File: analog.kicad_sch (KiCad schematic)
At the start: 37 parts, among them J2 Conn_02x01, J3 Conn_02x01, J4 Conn_02x01, J5 Conn_02x01, J6 Screw_Terminal_01x02, U2 INA241A1xD, U3 INA241A1xD, U4 INA241A1xD, U5 INA241A1xD, U6 ADS131A04, Y2 16.384 MHz

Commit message: Initial release A1
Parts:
- C25, C27: value 10pF -> 30pF
- R4, R5, R6, R7: value 13.7R -> 13R; footprint Resistor_SMD:R_1210_3225Metric -> libpt:R_1206_3216Metric
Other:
- note added: "Resistors should be .1%"
- note added: "Voltage range: 13*10G*.025A = 3.25V max .1^2 * 13 = 130 mW (before fuse trips)"
- note removed: "Re-check crystal footprint when crystal is chosen"
- note removed: "Voltage range: 13.7R*10G*.024A = 3.288V max .1^2 * 13.7 = 137 mW (before fuse trips)"
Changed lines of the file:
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@@
 	(title_block
 		(title "PT DAQ")
-		(date "2026-01-01")
+		(date "2026-01-12")
 		(rev "1A")
 		(company "Aggie Propulsion and Rocketry Lab")
@@
 		)
 	)
-	(text "Voltage range:\n13.7R*10G*.024A = 3.288V max\n.1^2 * 13.7 = 137 mW (before fuse trips)"
+	(text "Voltage range:\n13*10G*.025A = 3.25V max\n.1^2 * 13 = 130 mW (before fuse trips)"
 		(exclude_from_sim no)
 		(at 107.95 34.29 0)
@@
 		)
 	)
-	(text "Re-check crystal footprint when crystal is chosen"
+	(text "Resistors should be .1%"
 		(exclude_from_sim no)
-		(at 190.5 129.54 0)
+		(at 30.988 193.548 0)
 		(effects
 			(font
@@
 			)
 		)
-		(property "Value" "13.7R"
+		(property "Value" "13R"
 			(at 25.4 135.8899 0)
 			(effects
@@
 			)
 		)
-		(property "Footprint" "Resistor_SMD:R_1210_3225Metric"
+		(property "Footprint" "libpt:R_1206_3216Metric"
 			(at 22.86 134.62 0)
 			(effects
@@
 		(dnp no)
 		(property "Reference" "J5"
-			(at 21.336 166.37 90)
+			(at 28.956 166.624 90)
 			(effects
 				(font
@@
 			)
 		)
-		(property "Value" "13.7R"
+		(property "Value" "13R"
 			(at 25.4 92.7099 0)
 			(effects
@@
 			)
 		)
-		(property "Footprint" "Resistor_SMD:R_1210_3225Metric"
+		(property "Footprint" "libpt:R_1206_3216Metric"
 			(at 22.86 91.44 0)
 			(effects
@@
 			)
 		)
-		(property "Value" "10pF"
+		(property "Value" "30pF"
 			(at 195.58 140.9762 0)
 			(effects
@@
 		(dnp no)
 		(property "Reference" "J4"
-			(at 20.066 123.19 90)
+			(at 27.178 123.444 90)
 			(effects
 				(font
@@
 		(dnp no)
 		(property "Reference" "J3"
-			(at 20.066 80.01 90)
+			(at 27.178 79.756 90)
 			(effects
 				(font
@@
 			)
 		)
-		(property "Value" "13.7R"
+		(property "Value" "13R"
 			(at 26.67 179.0699 0)
 			(effects
@@
 			)
 		)
-		(property "Footprint" "Resistor_SMD:R_1210_3225Metric"
+		(property "Footprint" "libpt:R_1206_3216Metric"
 			(at 24.13 177.8 0)
 			(effects
@@
 			)
 		)
-		(property "Value" "13.7R"
+		(property "Value" "13R"
 			(at 24.13 49.5299 0)
 			(effects
@@
 			)
 		)
-		(property "Footprint" "Resistor_SMD:R_1210_3225Metric"
+		(property "Footprint" "libpt:R_1206_3216Metric"
 			(at 21.59 48.26 0)
 			(effects
@@
 		(dnp no)
 		(property "Reference" "J2"
-			(at 18.796 36.83 90)
+			(at 26.162 37.084 90)
 			(effects
 				(font
@@
 			)
 		)
-		(property "Value" "10pF"
+		(property "Value" "30pF"
 			(at 180.34 140.9762 0)
 			(effects

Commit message: Pranked by propfeed and engine again
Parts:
- removed C12, C13, C14, C15: 100nF, aprlprints:C_0603-noct, symbol Device:C_Small
- removed C16, C17, C18: 6.8nF, aprlprints:C_0603-noct, symbol Device:C_Small
- removed R10, R8: 330R, aprlprints:R_0603-noct, symbol Device:R_Small_US
- removed R5, R6, R7: 13R, libpt:R_1206_3216Metric, symbol Device:R_Small_US
- removed U2, U3, U4, U5: INA241A1xD, Package_SO:SOIC-8_3.9x4.9mm_P1.27mm, symbol Amplifier_Current:INA241A1xD
- added C25, C28, C31: 10nF, aprlprints:C_0603-noct, symbol Device:C_Small
- added NT1, NT2, NT3, NT4: NetTie_2, NetTie:NetTie-2_SMD_Pad0.5mm, symbol Device:NetTie_2
- added R12, R14, R15, R17, R18, R20: 100R, APRLPrints:R_0603, symbol Device:R_Small_US
- added R13, R16, R19: 100R, APRLPrints:R_0805, symbol Device:R_Small_US
- C19: value 6.8nF -> 10nF
- R10: renamed from R4; value 13R -> 100R; footprint libpt:R_1206_3216Metric -> APRLPrints:R_0805
- R11, R9: value 330R -> 100R; footprint aprlprints:R_0603-noct -> APRLPrints:R_0603
- renumbered C23 to C20, C24 to C21, C26 to C22, C28 to C23, C20 to C24, C21 to C26, C22 to C27, C25 to C29, C27 to C30, F1 to F2, J2 to J3, J3 to J4, J4 to J5, J5 to J6, J6 to J7, U6 to U4
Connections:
- net AIN1+: now also C19.1, R9.2
- net AIN2+: now also C25.1, R12.2; no longer R9.2
- net AIN3+: now also C28.1, R15.2
- net AIN4+: now also C31.1, R18.2; no longer C19.1, R11.2
- net GND: now also NT1.1, NT2.1, NT3.1, NT4.1; no longer C19.2, R10.2, U4.1 (AIN1N), U4.3 (AIN2N), U4.5 (AIN3N), U4.7 (AIN4N)
- net AIN3_SENSE+: now reaches J5.2 (Pin_2)
- net AIN3_SENSE+: now also R15.1, R16.1
- net AIN1_SENSE+: now reaches R9.1
- net AIN1_SENSE+: now also J3.2 (Pin_2), R10.1
- net AIN2_SENSE+: now reaches J4.2 (Pin_2)
- net AIN2_SENSE+: now also R12.1, R13.1
- net AIN4_SENSE+: now reaches J6.2 (Pin_2)
- net AIN4_SENSE+: now also R18.1, R19.1
- net AIN1_SENSE-: now reaches R11.1
- net AIN1_SENSE-: now also R10.2, NT1.2
- new net AIN1-: C19.2, R11.2, U4.1 (AIN1N)
- new net AIN2-: C25.2, R14.2, U4.3 (AIN2N)
- new net AIN2_SENSE-: NT3.2, R13.2, R14.1
- new net AIN3-: C28.2, R17.2, U4.5 (AIN3N)
- new net AIN3_SENSE-: NT2.2, R16.2, R17.1
- new net AIN4-: C31.2, R20.2, U4.7 (AIN4N)
- new net AIN4_SENSE-: NT4.2, R19.2, R20.1
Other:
- note added: "Max power is (0.022^2)*100 = 0.0484W"
- note added: "Normal range: 0 mA open/fault-low -> 0.000 V 4 mA -> 0.400 V = 0 psi 20 mA -> 2.000 V = 5000 psi 21.5 mA overrange -> 2.150 V Pressure scale: 16 mA span = 5000 psi 3.2 uA/psi 100 ohm * 3.2 uA/psi = 320 uV/psi 0.1 psi = 32 uV With internal VREF = 2.442 V, gain 1"
- note added: "Resistors should be 0.1% at worst"
- note added: "The differential-mode RC low-pass filter will require calibration to remove loading effects"
- note added: "c0g preferred f_c is 1/(2*pi*2R*C) = 79.6 kHz as for modulator: mratio = 4.096 MHz / 79.6 kHz - 51.5 so on log scale thats 34.2 dB attenuation but at 1 kSPS thats 500 Hz / 79.6 kHz - 0.0063"
- note removed: "OSR is 256 kHz decimated to 1 kHz 2x nyquist + some headroom -> ~72 kHz target f_c = 1/2*pi*R*C = 70.924 kHz"
- note removed: "Resistors should be .1%"
- note removed: "Voltage range: 13*10G*.025A = 3.25V max .1^2 * 13 = 130 mW (before fuse trips)"
- moved on the sheet: J3, J4, J5, J6, R10

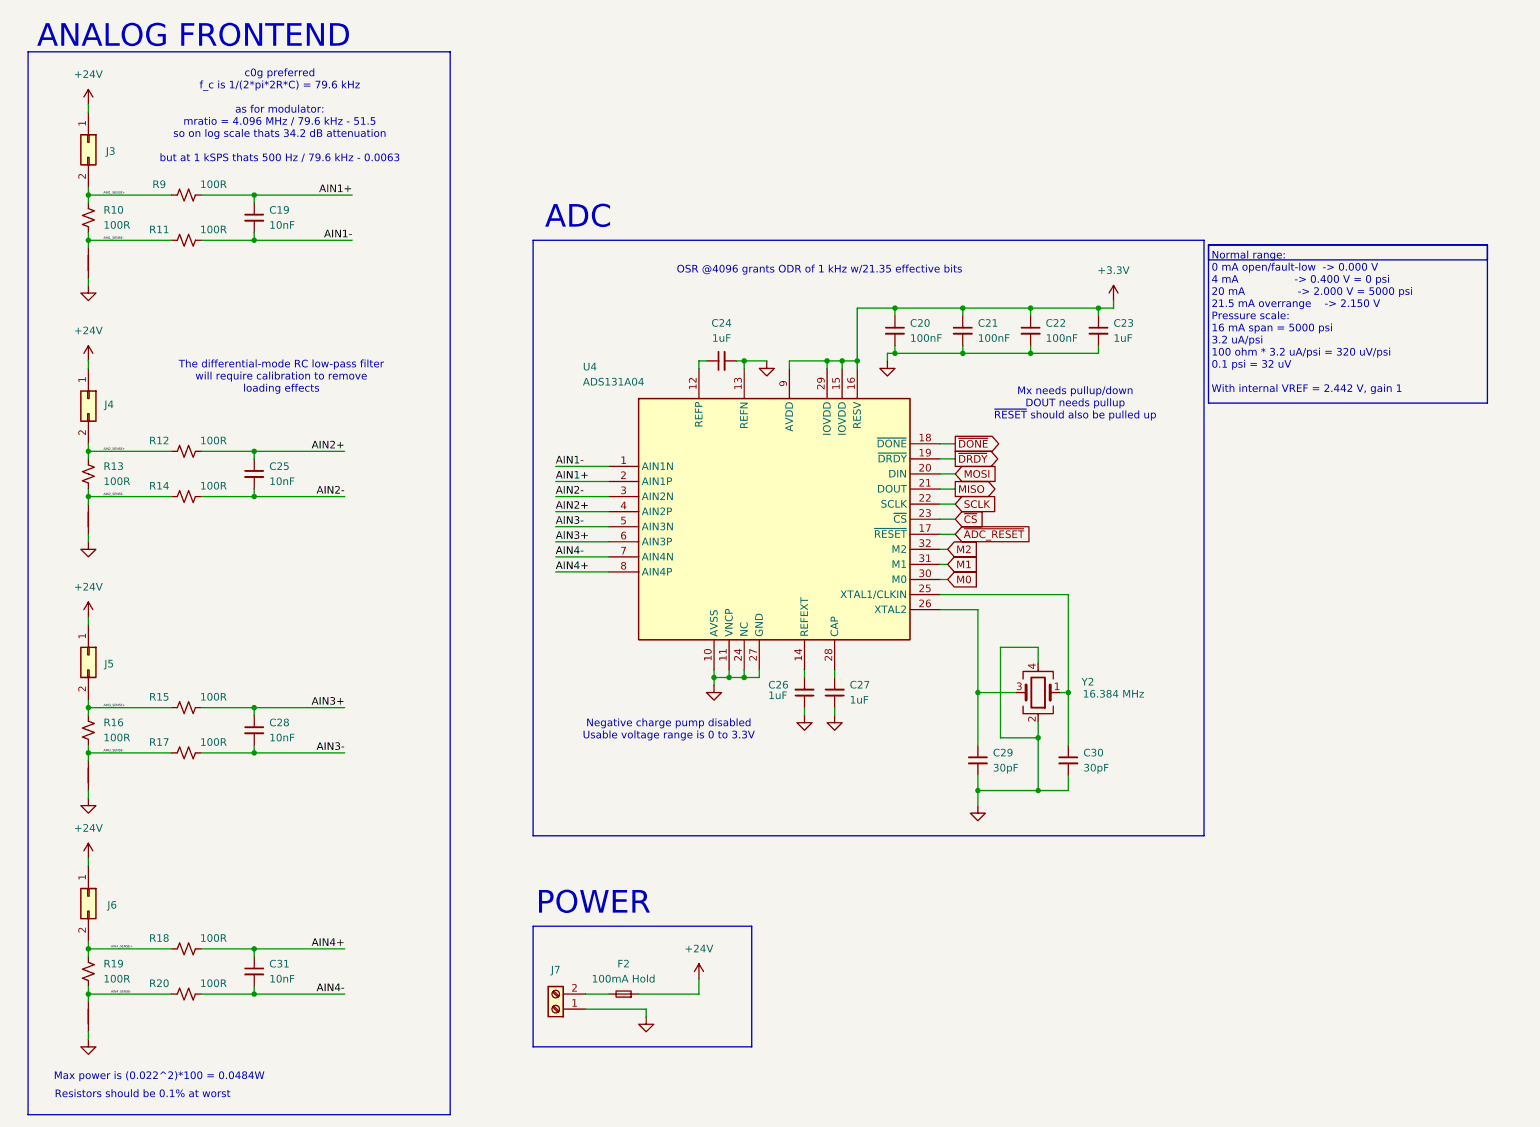
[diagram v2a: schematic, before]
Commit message: Swap TPS7A20 for LP5907 (Daniel yelled at me again)
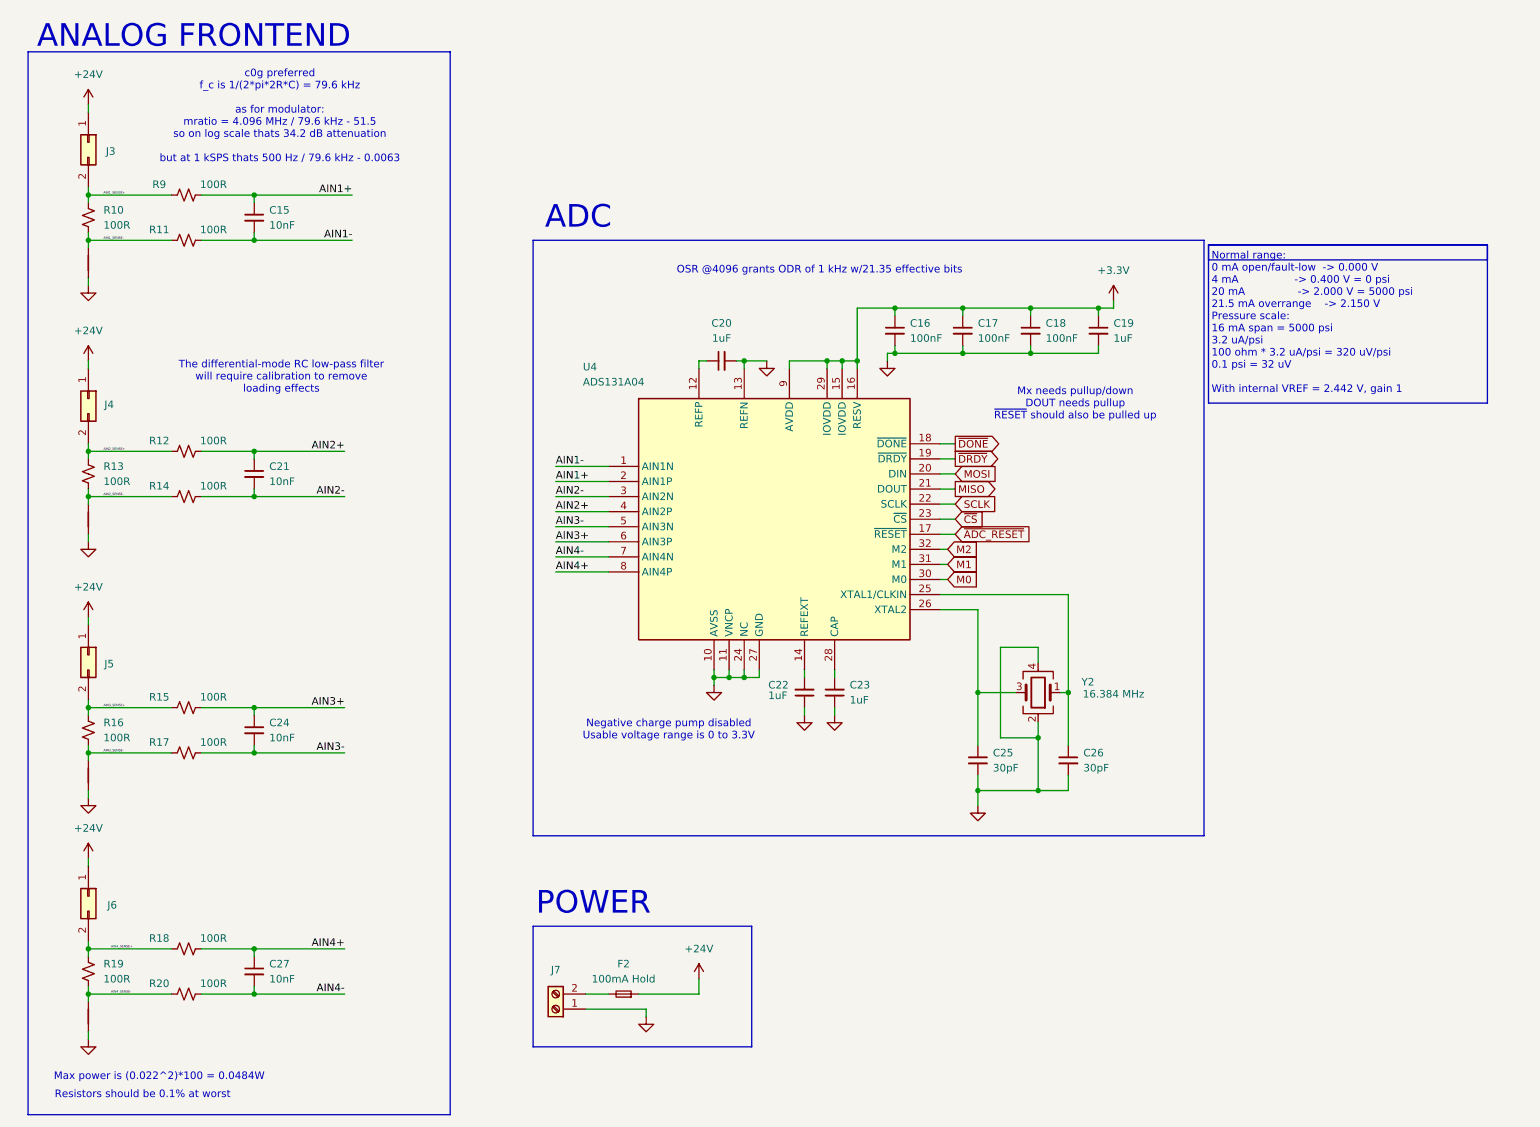
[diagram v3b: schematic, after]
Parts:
- renumbered C19 to C15, C20 to C16, C21 to C17, C22 to C18, C23 to C19, C24 to C20, C25 to C21, C26 to C22, C27 to C23, C28 to C24, C29 to C25, C30 to C26, C31 to C27, NT3 to NT2, NT2 to NT3
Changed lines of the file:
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@@
 		(dnp no)
 		(fields_autoplaced yes)
-		(property "Reference" "NT3"
+		(property "Reference" "NT2"
 			(at 22.86 99.06 0)
 			(hide yes)
@@
 			(project "PT"
 				(path "/0eb5ae8a-84ea-4b7e-bec4-bb4e0217d666/de3cef6c-f0bf-43f9-bc77-3e59044b84fe"
-					(reference "NT3")
+					(reference "NT2")
 					(unit 1)
 				)
@@
 		(dnp no)
 		(fields_autoplaced yes)
-		(property "Reference" "C22"
+		(property "Reference" "C18"
 			(at 189.23 66.0462 0)
 			(show_name no)
@@
 			(project "PT"
 				(path "/0eb5ae8a-84ea-4b7e-bec4-bb4e0217d666/de3cef6c-f0bf-43f9-bc77-3e59044b84fe"
-					(reference "C22")
+					(reference "C18")
 					(unit 1)
 				)
@@
 		(dnp no)
 		(fields_autoplaced yes)
-		(property "Reference" "C31"
+		(property "Reference" "C27"
 			(at 58.42 173.9962 0)
 			(show_name no)
@@
 			(project "PT"
 				(path "/0eb5ae8a-84ea-4b7e-bec4-bb4e0217d666/de3cef6c-f0bf-43f9-bc77-3e59044b84fe"
-					(reference "C31")
+					(reference "C27")
 					(unit 1)
 				)
@@
 		(dnp no)
 		(fields_autoplaced yes)
-		(property "Reference" "#PWR046"
+		(property "Reference" "#PWR045"
 			(at 121.92 189.23 0)
 			(hide yes)
@@
 			(project "PT"
 				(path "/0eb5ae8a-84ea-4b7e-bec4-bb4e0217d666/de3cef6c-f0bf-43f9-bc77-3e59044b84fe"
-					(reference "#PWR046")
+					(reference "#PWR045")
 					(unit 1)
 				)
@@
 		(in_pos_files yes)
 		(dnp no)
-		(property "Reference" "C26"
+		(property "Reference" "C22"
 			(at 142.494 127 0)
 			(show_name no)
@@
 			(project "PT"
 				(path "/0eb5ae8a-84ea-4b7e-bec4-bb4e0217d666/de3cef6c-f0bf-43f9-bc77-3e59044b84fe"
-					(reference "C26")
+					(reference "C22")
 					(unit 1)
 				)
@@
 		(dnp no)
 		(fields_autoplaced yes)
-		(property "Reference" "C27"
+		(property "Reference" "C23"
 			(at 156.21 126.9935 0)
 			(show_name no)
@@
 			(project "PT"
 				(path "/0eb5ae8a-84ea-4b7e-bec4-bb4e0217d666/de3cef6c-f0bf-43f9-bc77-3e59044b84fe"
-					(reference "C27")
+					(reference "C23")
 					(unit 1)
 				)
@@
 		(dnp no)
 		(fields_autoplaced yes)
-		(property "Reference" "NT2"
+		(property "Reference" "NT3"
 			(at 22.86 142.24 0)
 			(hide yes)
@@
 			(project "PT"
 				(path "/0eb5ae8a-84ea-4b7e-bec4-bb4e0217d666/de3cef6c-f0bf-43f9-bc77-3e59044b84fe"
-					(reference "NT2")
+					(reference "NT3")
 					(unit 1)
 				)
@@
 		(dnp no)
 		(fields_autoplaced yes)
-		(property "Reference" "C30"
+		(property "Reference" "C26"
 			(at 195.58 138.4362 0)
 			(show_name no)
@@
 			(project "PT"
 				(path "/0eb5ae8a-84ea-4b7e-bec4-bb4e0217d666/de3cef6c-f0bf-43f9-bc77-3e59044b84fe"
-					(reference "C30")
+					(reference "C26")
 					(unit 1)
 				)
@@
 		(dnp no)
 		(fields_autoplaced yes)
-		(property "Reference" "C28"
+		(property "Reference" "C24"
 			(at 58.42 133.3562 0)
 			(show_name no)
@@
 			(project "PT"
 				(path "/0eb5ae8a-84ea-4b7e-bec4-bb4e0217d666/de3cef6c-f0bf-43f9-bc77-3e59044b84fe"
-					(reference "C28")
+					(reference "C24")
 					(unit 1)
 				)
@@
 		(dnp no)
 		(fields_autoplaced yes)
-		(property "Reference" "C20"
+		(property "Reference" "C16"
 			(at 166.37 66.0462 0)
 			(show_name no)
@@
 			(project "PT"
 				(path "/0eb5ae8a-84ea-4b7e-bec4-bb4e0217d666/de3cef6c-f0bf-43f9-bc77-3e59044b84fe"
-					(reference "C20")
+					(reference "C16")
 					(unit 1)
 				)
@@
 		(dnp no)
 		(fields_autoplaced yes)
-		(property "Reference" "C21"
+		(property "Reference" "C17"
 			(at 177.8 66.0462 0)
 			(show_name no)
@@
 			(project "PT"
 				(path "/0eb5ae8a-84ea-4b7e-bec4-bb4e0217d666/de3cef6c-f0bf-43f9-bc77-3e59044b84fe"
-					(reference "C21")
+					(reference "C17")
 					(unit 1)
 				)
@@
 		(dnp no)
 		(fields_autoplaced yes)
-		(property "Reference" "C19"
+		(property "Reference" "C15"
 			(at 58.42 46.9962 0)
 			(show_name no)
@@
 			(project "PT"
 				(path "/0eb5ae8a-84ea-4b7e-bec4-bb4e0217d666/de3cef6c-f0bf-43f9-bc77-3e59044b84fe"
-					(reference "C19")
+					(reference "C15")
 					(unit 1)
 				)
@@
 		(dnp no)
 		(fields_autoplaced yes)
-		(property "Reference" "#PWR045"
+		(property "Reference" "#PWR046"
 			(at 27.94 193.04 0)
 			(hide yes)
@@
 			(project "PT"
 				(path "/0eb5ae8a-84ea-4b7e-bec4-bb4e0217d666/de3cef6c-f0bf-43f9-bc77-3e59044b84fe"
-					(reference "#PWR045")
+					(reference "#PWR046")
 					(unit 1)
 				)
@@
 		(dnp no)
 		(fields_autoplaced yes)
-		(property "Reference" "C29"
+		(property "Reference" "C25"
 			(at 180.34 138.4362 0)
 			(show_name no)
@@
 			(project "PT"
 				(path "/0eb5ae8a-84ea-4b7e-bec4-bb4e0217d666/de3cef6c-f0bf-43f9-bc77-3e59044b84fe"
-					(reference "C29")
+					(reference "C25")
 					(unit 1)
 				)
@@
 		(dnp no)
 		(fields_autoplaced yes)
-		(property "Reference" "C25"
+		(property "Reference" "C21"
 			(at 58.42 90.1762 0)
 			(show_name no)
@@
 			(project "PT"
 				(path "/0eb5ae8a-84ea-4b7e-bec4-bb4e0217d666/de3cef6c-f0bf-43f9-bc77-3e59044b84fe"
-					(reference "C25")
+					(reference "C21")
 					(unit 1)
 				)
@@
 		(dnp no)
 		(fields_autoplaced yes)
-		(property "Reference" "C24"
+		(property "Reference" "C20"
 			(at 134.6263 66.04 90)
 			(show_name no)
@@
 			(project "PT"
 				(path "/0eb5ae8a-84ea-4b7e-bec4-bb4e0217d666/de3cef6c-f0bf-43f9-bc77-3e59044b84fe"
-					(reference "C24")
+					(reference "C20")
 					(unit 1)
 				)
@@
 		(dnp no)
 		(fields_autoplaced yes)
-		(property "Reference" "C23"
+		(property "Reference" "C19"
 			(at 200.66 66.0462 0)
 			(show_name no)
@@
 			(project "PT"
 				(path "/0eb5ae8a-84ea-4b7e-bec4-bb4e0217d666/de3cef6c-f0bf-43f9-bc77-3e59044b84fe"
-					(reference "C23")
+					(reference "C19")
 					(unit 1)
 				)

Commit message: Swap to STM32H563RIV6, and add split +3.3V and +3.3VA
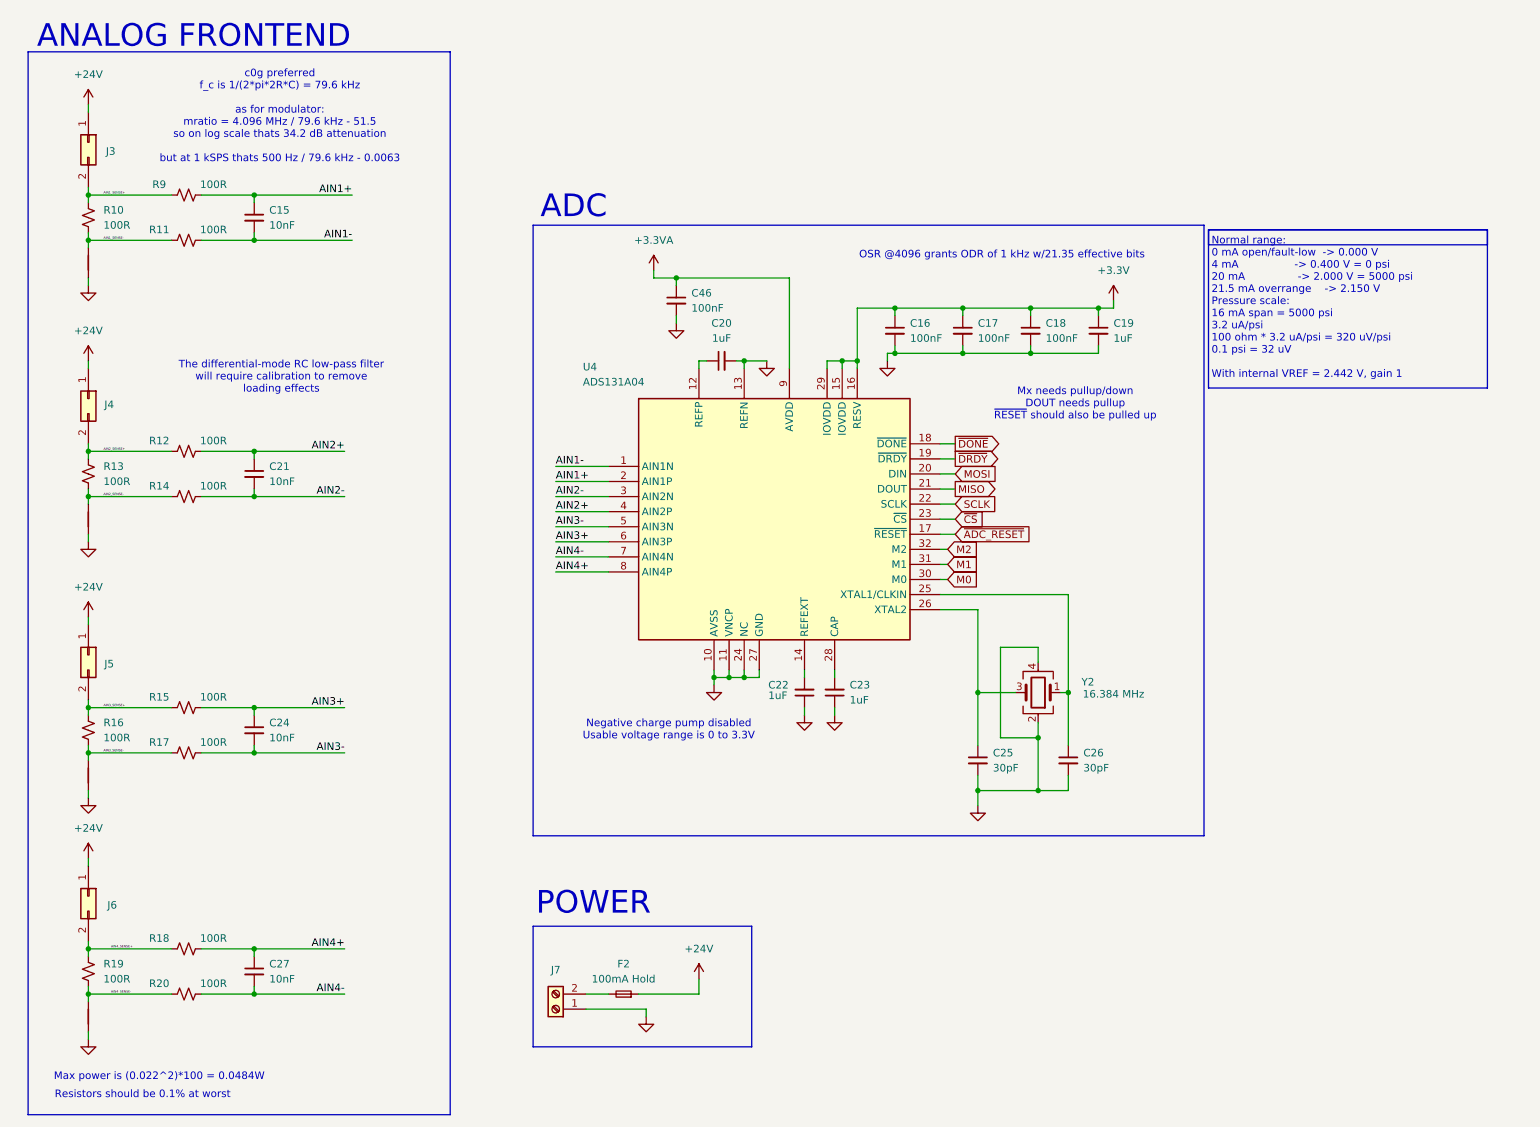
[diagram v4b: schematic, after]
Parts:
- added C46: 100nF, aprlprints:C_0603-noct, symbol Device:C_Small
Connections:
- net +3.3V: no longer U4.9 (AVDD)
- net GND: now also C46.2
- new net +3.3VA: C46.1, U4.9 (AVDD)
